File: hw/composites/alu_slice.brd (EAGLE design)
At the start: 50 x 50 mm, 9 parts, among them CON2 GENERIC-2X10

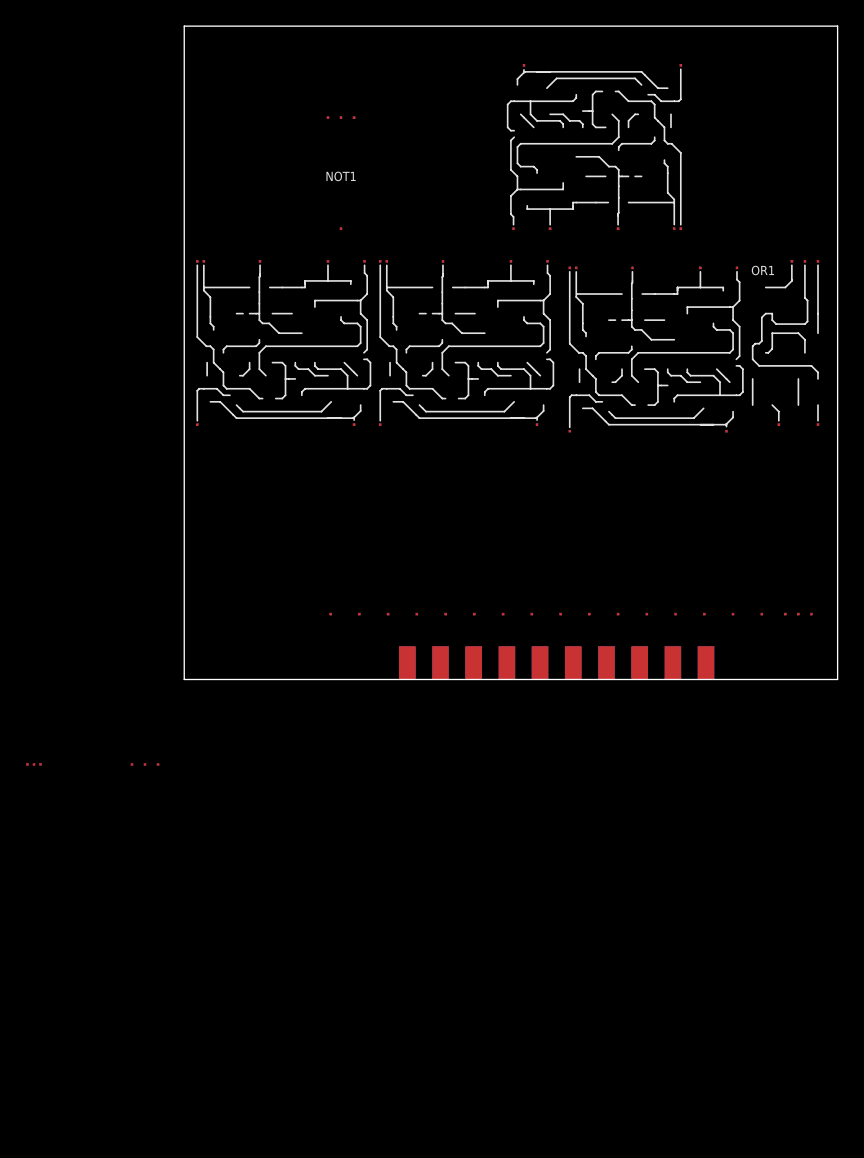
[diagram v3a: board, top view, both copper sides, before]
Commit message: adds additional tests for offloading of CMP on slice
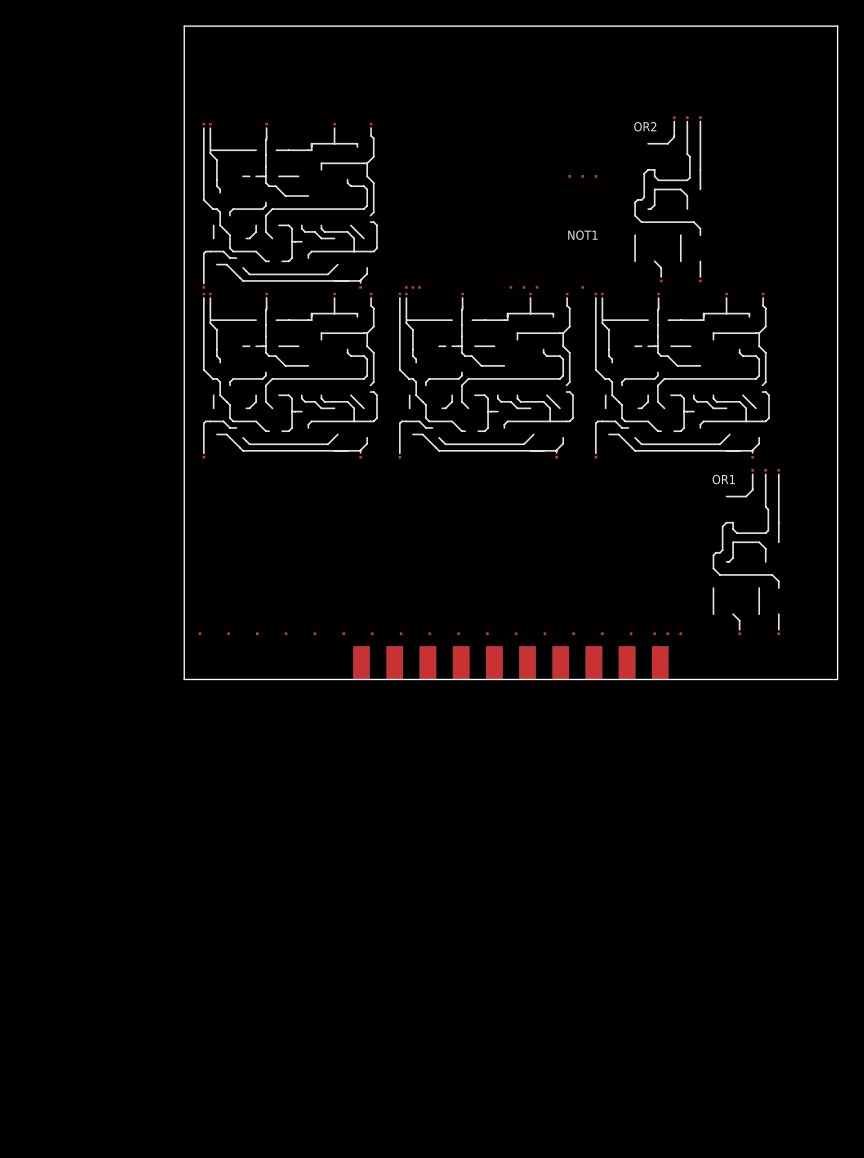
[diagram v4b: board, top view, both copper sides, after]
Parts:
- added OR2: OR, p.peter-gator:OR
- moved SEL1 46.6 mm to (16.0, 30.0)
- moved XOR2 41.2 mm to (1.00, 30.0), turned to 0 degrees
- moved NOT1 19.0 mm to (28.5, 30.0)
- moved OR1 16.3 mm to (39.5, 3.50)
- moved SEL2 10.1 mm to (0.00, 3.50)
- moved CON2 3.50 mm to (25.0, 0.00)
- moved XOR3 2.92 mm to (16.0, 17.0)
- moved XOR4 2.83 mm to (31.0, 17.0)
- moved XOR1 2.55 mm to (1.00, 17.0)
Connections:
- new net _EQUAL_IN: CON2.15, OR2.A
- new net _EQUAL_OUT: CON2.19, OR2.OR
- net +5V: now also OR2._VP
- net GND: now also OR2._VN
- net NC: no longer CON2.15, CON2.18
- net RESULT: now also CON2.18; no longer CON2.19
- net SUM: now also OR2.B

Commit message: cleans up board layout
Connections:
- removed net NC: CON2.16
- net S_LOAD: now also CON2.16
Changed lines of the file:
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@@
 <signal name="S_LOAD">
 <contactref element="SEL2" pad="S2"/>
+<contactref element="CON2" pad="16"/>
+<wire x1="5.6" y1="3.5" x2="31.35" y2="1.27" width="0" layer="19" extent="1-1"/>
 </signal>
 <signal name="S_ID">
@@
 <signal name="N$4">
 </signal>
-<signal name="NC">
-<contactref element="CON2" pad="16"/>
-</signal>
 <signal name="INVERT_OUT">

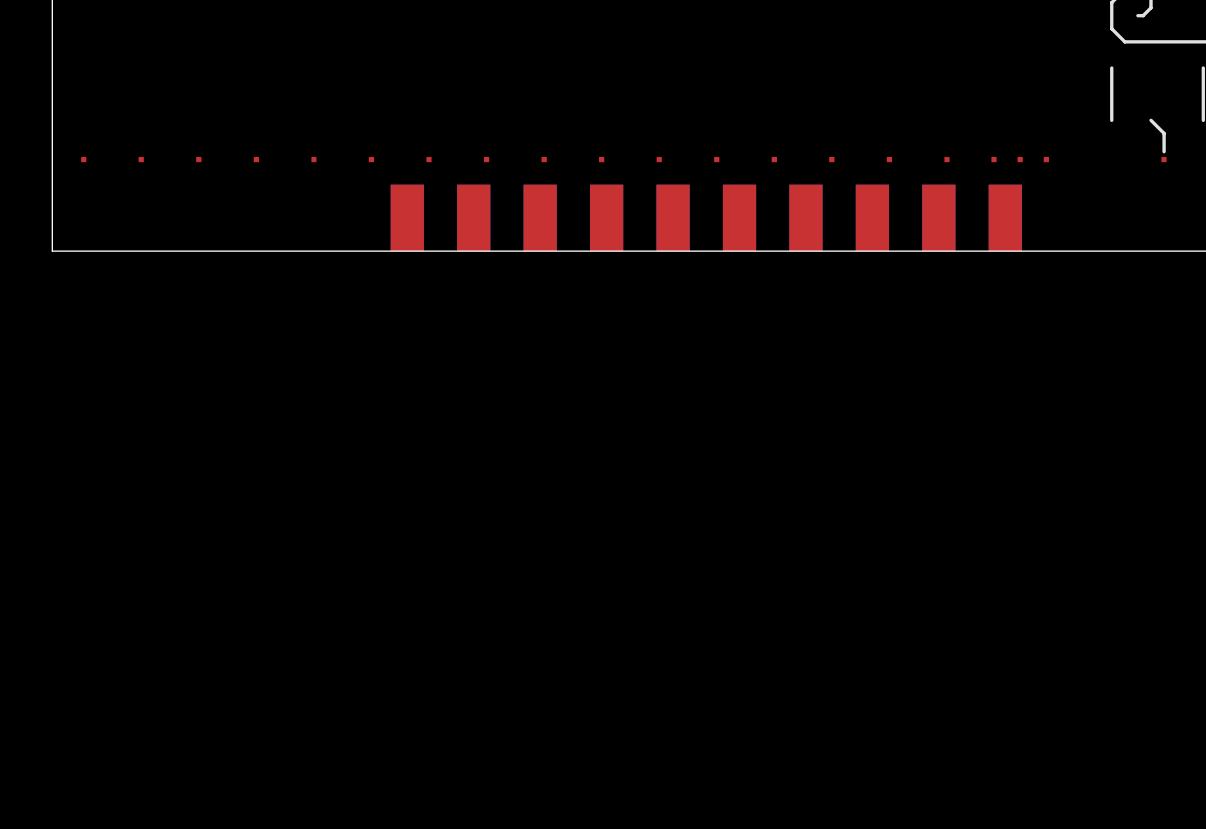
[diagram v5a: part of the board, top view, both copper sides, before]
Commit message: changes CMP and ID to use same selector
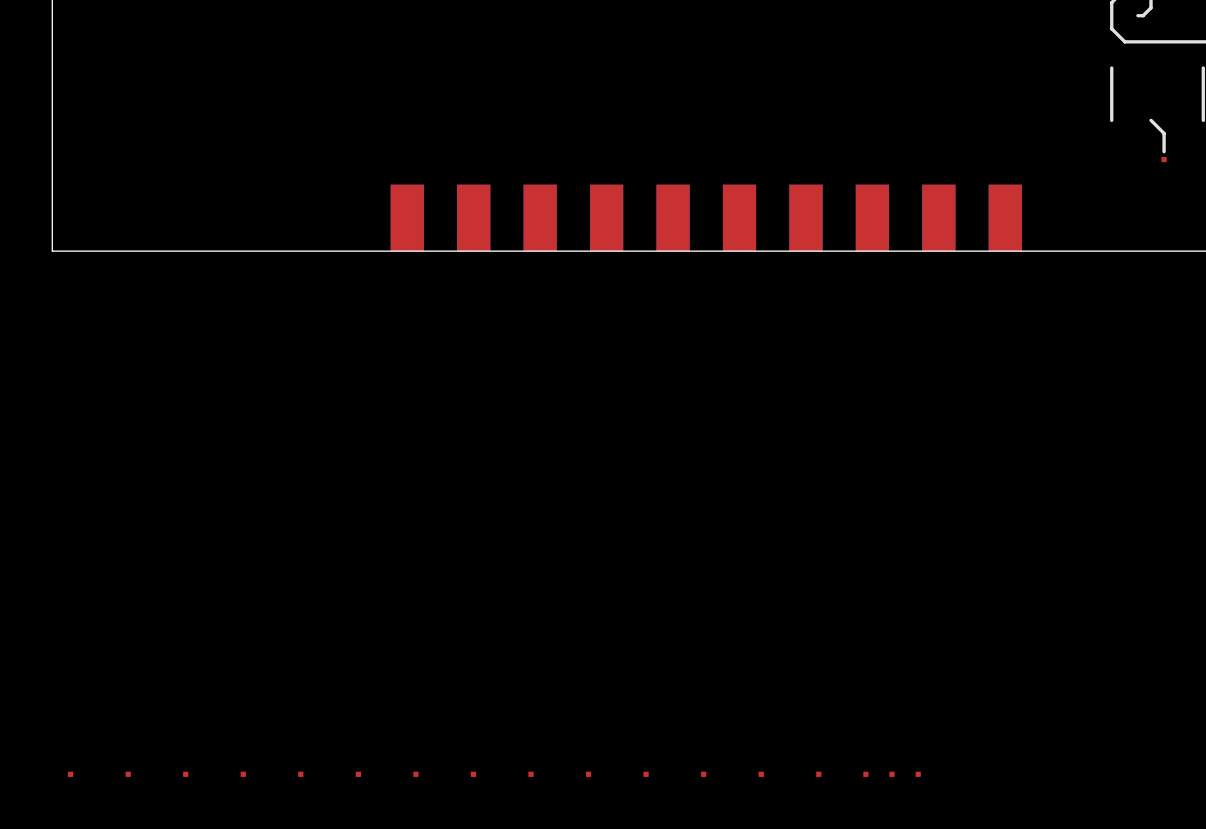
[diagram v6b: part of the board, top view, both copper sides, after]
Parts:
- removed SEL2: 8_BIT_SELECT, p.peter-gator:SELECTOR-8_BIT-NOMUX
- added SEL3: 7_VAL_SELECT, p.peter-gator:SELECTOR-7_BIT-NOMUX
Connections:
- removed net S_CMP: SEL2.S3
- net +5V: now also SEL3._VP; no longer SEL2._VP
- net A: now also SEL3.I3; no longer SEL2.I3, SEL2.I4
- net AND: now also SEL3.I7; no longer SEL2.I8
- net B: now also SEL3.I2; no longer SEL2.I2
- net GND: now also SEL3._VN; no longer SEL2._VN
- net N$1: now also SEL3.OUT; no longer SEL2.OUT
- net N$3: now also SEL3.I6; no longer SEL2.I7
- net N$5: now also SEL3.I1; no longer SEL2.I1
- net SUM: now also SEL3.I4; no longer SEL2.I5
- net S_ADD: now also SEL3.S4; no longer SEL2.S5
- net S_AND: now also SEL3.S7; no longer SEL2.S8
- net S_ID: now also SEL3.S3; no longer SEL2.S4
- net S_LOAD: now also SEL3.S2; no longer SEL2.S2
- net S_OR: now also SEL3.S6; no longer SEL2.S7
- net S_SHIFT: now also SEL3.S1; no longer SEL2.S1
- net S_XOR: now also SEL3.S5; no longer SEL2.S6
- net XOR: now also SEL3.I5; no longer SEL2.I6
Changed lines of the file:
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@@
 <element name="XOR3" library="p.peter-gator" package="XOR" value="XOR" x="16" y="17"/>
 <element name="OR1" library="p.peter-gator" package="OR" value="OR" x="39.5" y="3.5"/>
-<element name="SEL2" library="p.peter-gator" package="SELECTOR-8_BIT-NOMUX" value="8_BIT_SELECT" x="0" y="3.5"/>
 <element name="CON2" library="p.peter-connectors" package="PINHEADER-100MIL-2X10-EDGE" value="GENERIC-2X10" x="25" y="0"/>
 <element name="XOR1" library="p.peter-gator" package="XOR" value="XOR" x="1" y="17"/>
@@
 <element name="SEL1" library="p.peter-gator" package="SELECTOR-2-LANE-NOMUX" value="1_BIT_SELECT" x="16" y="30"/>
 <element name="OR2" library="p.peter-gator" package="OR" value="OR" x="33.5" y="30.5"/>
+<element name="SEL3" library="p.peter-gator" package="SELECTOR-7_BIT-NOMUX" value="7_VAL_SELECT" x="-0.5" y="-20"/>
 </elements>
 <signals>
 <signal name="A">
 <contactref element="XOR2" pad="A"/>
-<contactref element="SEL2" pad="I4"/>
 <contactref element="CON2" pad="1"/>
-<contactref element="SEL2" pad="I3"/>
-<wire x1="12.2" y1="3.5" x2="13.5" y2="30" width="0" layer="19" extent="1-1"/>
-<wire x1="13.57" y1="1.27" x2="12.2" y2="3.5" width="0" layer="19" extent="1-16"/>
-<wire x1="16.6" y1="3.5" x2="13.57" y2="1.27" width="0" layer="19" extent="1-16"/>
+<contactref element="SEL3" pad="I3"/>
+<wire x1="13.57" y1="1.27" x2="13.5" y2="30" width="0" layer="19" extent="1-16"/>
+<wire x1="11.7" y1="-20" x2="13.57" y2="1.27" width="0" layer="19" extent="1-16"/>
 </signal>
 <signal name="XOR">
 <contactref element="XOR3" pad="B"/>
 <contactref element="XOR2" pad="XOR"/>
-<contactref element="SEL2" pad="I6"/>
+<contactref element="SEL3" pad="I5"/>
 <wire x1="16.5" y1="17" x2="11.5" y2="42.5" width="0" layer="19" extent="1-1"/>
-<wire x1="25.4" y1="3.5" x2="16.5" y2="17" width="0" layer="19" extent="1-1"/>
+<wire x1="20.5" y1="-20" x2="16.5" y2="17" width="0" layer="19" extent="1-1"/>
 </signal>
 <signal name="CARRY_IN">
@@
 </signal>
 <signal name="SUM">
-<contactref element="SEL2" pad="I5"/>
 <contactref element="XOR3" pad="XOR"/>
 <contactref element="OR2" pad="B"/>
-<wire x1="21" y1="3.5" x2="26.5" y2="29.5" width="0" layer="19" extent="1-1"/>
-<wire x1="39.5" y1="30.5" x2="21" y2="3.5" width="0" layer="19" extent="1-1"/>
+<contactref element="SEL3" pad="I4"/>
+<wire x1="26.5" y1="29.5" x2="39.5" y2="30.5" width="0" layer="19" extent="1-1"/>
+<wire x1="16.1" y1="-20" x2="26.5" y2="29.5" width="0" layer="19" extent="1-1"/>
 </signal>
 <signal name="CARRY_OUT">
@@
 <contactref element="XOR3" pad="_VP"/>
 <contactref element="OR1" pad="_VP"/>
-<contactref element="SEL2" pad="_VP"/>
 <contactref element="CON2" pad="2"/>
 <contactref element="XOR1" pad="_VP"/>
@@
 <contactref element="SEL1" pad="_VP"/>
 <contactref element="OR2" pad="_VP"/>
+<contactref element="SEL3" pad="_VP"/>
+<wire x1="31.5" y1="38.5" x2="39.5" y2="43" width="0" layer="19" extent="1-1"/>
 <wire x1="32" y1="29.5" x2="31.5" y2="38.5" width="0" layer="19" extent="1-1"/>
 <wire x1="27" y1="30" x2="32" y2="29.5" width="0" layer="19" extent="1-1"/>
@@
 <wire x1="2" y1="42.5" x2="2" y2="29.5" width="0" layer="19" extent="1-1"/>
 <wire x1="45.5" y1="16" x2="32" y2="29.5" width="0" layer="19" extent="1-1"/>
-<wire x1="38" y1="3.5" x2="45.5" y2="16" width="0" layer="19" extent="1-1"/>
-<wire x1="39.5" y1="43" x2="2" y2="29.5" width="0" layer="19" extent="1-1"/>
-<wire x1="13.57" y1="1.27" x2="39.5" y2="43" width="0" layer="19" extent="1-1"/>
+<wire x1="13.57" y1="1.27" x2="17" y2="29.5" width="0" layer="19" extent="1-1"/>
+<wire x1="33.1" y1="-20" x2="13.57" y2="1.27" width="0" layer="19" extent="1-1"/>
 </signal>
 <signal name="GND">
@@
 <contactref element="XOR3" pad="_VN"/>
 <contactref element="OR1" pad="_VN"/>
-<contactref element="SEL2" pad="_VN"/>
 <contactref element="CON2" pad="20"/>
 <contactref element="XOR1" pad="_VN"/>
@@
 <contactref element="SEL1" pad="_VN"/>
 <contactref element="OR2" pad="_VN"/>
-<wire x1="44.5" y1="16" x2="44.3" y2="29.5" width="0" layer="19" extent="1-1"/>
-<wire x1="29.3" y1="29.5" x2="44.3" y2="29.5" width="0" layer="19" extent="1-1"/>
+<contactref element="SEL3" pad="_VN"/>
+<wire x1="30.5" y1="38.5" x2="38.5" y2="43" width="0" layer="19" extent="1-1"/>
+<wire x1="29.3" y1="29.5" x2="30.5" y2="38.5" width="0" layer="19" extent="1-1"/>
 <wire x1="25" y1="30" x2="29.3" y2="29.5" width="0" layer="19" extent="1-1"/>
-<wire x1="30.5" y1="38.5" x2="29.3" y2="29.5" width="0" layer="19" extent="1-1"/>
 <wire x1="14.3" y1="29.5" x2="25" y2="30" width="0" layer="19" extent="1-1"/>
 <wire x1="14.3" y1="42.5" x2="14.3" y2="29.5" width="0" layer="19" extent="1-1"/>
-<wire x1="36" y1="3.5" x2="44.5" y2="16" width="0" layer="19" extent="1-1"/>
-<wire x1="36.43" y1="1.27" x2="36" y2="3.5" width="0" layer="19" extent="1-1"/>
-<wire x1="38.5" y1="43" x2="14.3" y2="29.5" width="0" layer="19" extent="1-1"/>
+<wire x1="44.3" y1="29.5" x2="38.5" y2="43" width="0" layer="19" extent="1-1"/>
+<wire x1="44.5" y1="16" x2="44.3" y2="29.5" width="0" layer="19" extent="1-1"/>
+<wire x1="36.43" y1="1.27" x2="44.5" y2="16" width="0" layer="19" extent="1-1"/>
+<wire x1="31.1" y1="-20" x2="36.43" y2="1.27" width="0" layer="19" extent="1-1"/>
 </signal>
 <signal name="NOR">
@@
 </signal>
 <signal name="B">
-<contactref element="SEL2" pad="I2"/>
 <contactref element="CON2" pad="3"/>
 <contactref element="XOR4" pad="A"/>
+<contactref element="SEL3" pad="I2"/>
 <wire x1="16.11" y1="1.27" x2="43.5" y2="17" width="0" layer="19" extent="1-16"/>
-<wire x1="7.8" y1="3.5" x2="16.11" y2="1.27" width="0" layer="19" extent="1-16"/>
+<wire x1="7.3" y1="-20" x2="16.11" y2="1.27" width="0" layer="19" extent="1-16"/>
 </signal>
 <signal name="AND">
 <contactref element="OR1" pad="B"/>
 <contactref element="XOR2" pad="AND"/>
-<contactref element="SEL2" pad="I8"/>
-<wire x1="45.5" y1="3.5" x2="1.5" y2="42.5" width="0" layer="19" extent="1-1"/>
-<wire x1="34.2" y1="3.5" x2="45.5" y2="3.5" width="0" layer="19" extent="1-1"/>
+<contactref element="SEL3" pad="I7"/>
+<wire x1="29.3" y1="-20" x2="45.5" y2="3.5" width="0" layer="19" extent="1-1"/>
+<wire x1="1.5" y1="42.5" x2="45.5" y2="3.5" width="0" layer="19" extent="1-1"/>
 </signal>
 <signal name="N$8">
@@
 </signal>
 <signal name="S_OR">
-<contactref element="SEL2" pad="S7"/>
 <contactref element="CON2" pad="10"/>
-<wire x1="23.73" y1="1.27" x2="27.6" y2="3.5" width="0" layer="19" extent="1-1"/>
+<contactref element="SEL3" pad="S6"/>
+<wire x1="22.7" y1="-20" x2="23.73" y2="1.27" width="0" layer="19" extent="1-1"/>
 </signal>
 <signal name="S_XOR">
-<contactref element="SEL2" pad="S6"/>
 <contactref element="CON2" pad="12"/>
-<wire x1="26.27" y1="1.27" x2="23.2" y2="3.5" width="0" layer="19" extent="1-1"/>
+<contactref element="SEL3" pad="S5"/>
+<wire x1="18.3" y1="-20" x2="26.27" y2="1.27" width="0" layer="19" extent="1-1"/>
 </signal>
 <signal name="S_ADD">
-<contactref element="SEL2" pad="S5"/>
 <contactref element="CON2" pad="8"/>
-<wire x1="21.19" y1="1.27" x2="18.8" y2="3.5" width="0" layer="19" extent="1-1"/>
-</signal>
-<signal name="S_CMP">
-<contactref element="SEL2" pad="S3"/>
+<contactref element="SEL3" pad="S4"/>
+<wire x1="13.9" y1="-20" x2="21.19" y2="1.27" width="0" layer="19" extent="1-1"/>
 </signal>
 <signal name="S_LOAD">
-<contactref element="SEL2" pad="S2"/>
 <contactref element="CON2" pad="16"/>
-<wire x1="5.6" y1="3.5" x2="31.35" y2="1.27" width="0" layer="19" extent="1-1"/>
+<contactref element="SEL3" pad="S2"/>
+<wire x1="5.1" y1="-20" x2="31.35" y2="1.27" width="0" layer="19" extent="1-1"/>
 </signal>
 <signal name="S_ID">
-<contactref element="SEL2" pad="S4"/>
 <contactref element="CON2" pad="4"/>
-<wire x1="16.11" y1="1.27" x2="14.4" y2="3.5" width="0" layer="19" extent="1-1"/>
+<contactref element="SEL3" pad="S3"/>
+<wire x1="9.5" y1="-20" x2="16.11" y2="1.27" width="0" layer="19" extent="1-1"/>
 </signal>
 <signal name="S_AND">
-<contactref element="SEL2" pad="S8"/>
 <contactref element="CON2" pad="6"/>
-<wire x1="18.65" y1="1.27" x2="32" y2="3.5" width="0" layer="19" extent="1-1"/>
+<contactref element="SEL3" pad="S7"/>
+<wire x1="27.1" y1="-20" x2="18.65" y2="1.27" width="0" layer="19" extent="1-1"/>
 </signal>
 <signal name="S_SHIFT">
-<contactref element="SEL2" pad="S1"/>
 <contactref element="CON2" pad="14"/>
-<wire x1="1.2" y1="3.5" x2="28.81" y2="1.27" width="0" layer="19" extent="1-1"/>
+<contactref element="SEL3" pad="S1"/>
+<wire x1="0.7" y1="-20" x2="28.81" y2="1.27" width="0" layer="19" extent="1-1"/>
 </signal>
 <signal name="RESULT">
@@
 </signal>
 <signal name="N$1">
-<contactref element="SEL2" pad="OUT"/>
 <contactref element="XOR1" pad="A"/>
-<wire x1="13.5" y1="17" x2="37" y2="3.5" width="0" layer="19" extent="1-1"/>
+<contactref element="SEL3" pad="OUT"/>
+<wire x1="32.1" y1="-20" x2="13.5" y2="17" width="0" layer="19" extent="1-1"/>
 </signal>
 <signal name="N$2">
@@
 </signal>
 <signal name="N$3">
-<contactref element="SEL2" pad="I7"/>
 <contactref element="NOT1" pad="NOT"/>
-<wire x1="29.5" y1="38.5" x2="29.8" y2="3.5" width="0" layer="19" extent="1-1"/>
+<contactref element="SEL3" pad="I6"/>
+<wire x1="24.9" y1="-20" x2="29.5" y2="38.5" width="0" layer="19" extent="1-1"/>
 </signal>
 <signal name="N$5">
-<contactref element="SEL2" pad="I1"/>
 <contactref element="SEL1" pad="OUT"/>
-<wire x1="26" y1="30" x2="3.4" y2="3.5" width="0" layer="19" extent="1-1"/>
+<contactref element="SEL3" pad="I1"/>
+<wire x1="2.9" y1="-20" x2="26" y2="30" width="0" layer="19" extent="1-1"/>
 </signal>
 <signal name="RIGHT_A">
